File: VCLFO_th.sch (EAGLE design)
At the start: 38 parts, among them IC1 LM324N, IC3 LM358N

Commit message: Updated component values of LED2 and LDR1 (Vactrol/optocoupler).
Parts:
- LDR1: value PGM55xx 18-50k e-kit 40850005 -> Token PGM5539
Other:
- note added: "LED for LDR1 (DIY vactrol) Optosupply OSW50K57E1A White 5mm flat-front LED 2180-3000mcd"
- note removed: "LED for LDR1 (DIY vactrol)"
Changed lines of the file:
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@@
 <grid distance="0.1" unitdist="inch" unit="inch" style="lines" multiple="1" display="no" altdistance="0.01" altunitdist="inch" altunit="inch"/>
 <layers>
-<layer number="1" name="Top" color="4" fill="1" visible="yes" active="no"/>
-<layer number="16" name="Bottom" color="1" fill="1" visible="yes" active="no"/>
-<layer number="17" name="Pads" color="2" fill="1" visible="yes" active="no"/>
-<layer number="18" name="Vias" color="2" fill="1" visible="yes" active="no"/>
-<layer number="19" name="Unrouted" color="6" fill="1" visible="yes" active="no"/>
-<layer number="20" name="Dimension" color="15" fill="1" visible="yes" active="no"/>
-<layer number="21" name="tPlace" color="7" fill="1" visible="yes" active="no"/>
-<layer number="22" name="bPlace" color="7" fill="1" visible="yes" active="no"/>
-<layer number="23" name="tOrigins" color="15" fill="1" visible="yes" active="no"/>
-<layer number="24" name="bOrigins" color="15" fill="1" visible="yes" active="no"/>
-<layer number="25" name="tNames" color="7" fill="1" visible="yes" active="no"/>
-<layer number="26" name="bNames" color="7" fill="1" visible="yes" active="no"/>
-<layer number="27" name="tValues" color="7" fill="1" visible="yes" active="no"/>
-<layer number="28" name="bValues" color="7" fill="1" visible="yes" active="no"/>
+<layer number="1" name="Top" color="4" fill="1" visible="no" active="no"/>
+<layer number="16" name="Bottom" color="1" fill="1" visible="no" active="no"/>
+<layer number="17" name="Pads" color="2" fill="1" visible="no" active="no"/>
+<layer number="18" name="Vias" color="2" fill="1" visible="no" active="no"/>
+<layer number="19" name="Unrouted" color="6" fill="1" visible="no" active="no"/>
+<layer number="20" name="Dimension" color="15" fill="1" visible="no" active="no"/>
+<layer number="21" name="tPlace" color="7" fill="1" visible="no" active="no"/>
+<layer number="22" name="bPlace" color="7" fill="1" visible="no" active="no"/>
+<layer number="23" name="tOrigins" color="15" fill="1" visible="no" active="no"/>
+<layer number="24" name="bOrigins" color="15" fill="1" visible="no" active="no"/>
+<layer number="25" name="tNames" color="7" fill="1" visible="no" active="no"/>
+<layer number="26" name="bNames" color="7" fill="1" visible="no" active="no"/>
+<layer number="27" name="tValues" color="7" fill="1" visible="no" active="no"/>
+<layer number="28" name="bValues" color="7" fill="1" visible="no" active="no"/>
 <layer number="29" name="tStop" color="7" fill="3" visible="no" active="no"/>
 <layer number="30" name="bStop" color="7" fill="6" visible="no" active="no"/>
@@
 <layer number="35" name="tGlue" color="7" fill="4" visible="no" active="no"/>
 <layer number="36" name="bGlue" color="7" fill="5" visible="no" active="no"/>
-<layer number="37" name="tTest" color="7" fill="1" visible="yes" active="no"/>
-<layer number="38" name="bTest" color="7" fill="1" visible="yes" active="no"/>
+<layer number="37" name="tTest" color="7" fill="1" visible="no" active="no"/>
+<layer number="38" name="bTest" color="7" fill="1" visible="no" active="no"/>
 <layer number="39" name="tKeepout" color="4" fill="11" visible="no" active="no"/>
 <layer number="40" name="bKeepout" color="1" fill="11" visible="no" active="no"/>
@@
 <layer number="44" name="Drills" color="7" fill="1" visible="no" active="no"/>
 <layer number="45" name="Holes" color="7" fill="1" visible="no" active="no"/>
-<layer number="46" name="Milling" color="3" fill="1" visible="yes" active="no"/>
-<layer number="47" name="Measures" color="7" fill="1" visible="yes" active="no"/>
-<layer number="48" name="Document" color="7" fill="1" visible="yes" active="no"/>
-<layer number="49" name="Reference" color="7" fill="1" visible="yes" active="no"/>
-<layer number="50" name="dxf" color="7" fill="1" visible="yes" active="no"/>
-<layer number="51" name="tDocu" color="7" fill="1" visible="yes" active="no"/>
-<layer number="52" name="bDocu" color="7" fill="1" visible="yes" active="no"/>
-<layer number="53" name="tGND_GNDA" color="7" fill="1" visible="yes" active="no"/>
-<layer number="54" name="bGND_GNDA" color="7" fill="1" visible="yes" active="no"/>
-<layer number="56" name="wert" color="7" fill="1" visible="yes" active="no"/>
-<layer number="57" name="tCAD" color="7" fill="1" visible="yes" active="no"/>
+<layer number="46" name="Milling" color="3" fill="1" visible="no" active="no"/>
+<layer number="47" name="Measures" color="7" fill="1" visible="no" active="no"/>
+<layer number="48" name="Document" color="7" fill="1" visible="no" active="no"/>
+<layer number="49" name="Reference" color="7" fill="1" visible="no" active="no"/>
+<layer number="50" name="dxf" color="7" fill="1" visible="no" active="no"/>
+<layer number="51" name="tDocu" color="7" fill="1" visible="no" active="no"/>
+<layer number="52" name="bDocu" color="7" fill="1" visible="no" active="no"/>
+<layer number="53" name="tGND_GNDA" color="7" fill="1" visible="no" active="no"/>
+<layer number="54" name="bGND_GNDA" color="7" fill="1" visible="no" active="no"/>
+<layer number="56" name="wert" color="7" fill="1" visible="no" active="no"/>
+<layer number="57" name="tCAD" color="7" fill="1" visible="no" active="no"/>
 <layer number="90" name="Modules" color="5" fill="1" visible="yes" active="yes"/>
 <layer number="91" name="Nets" color="2" fill="1" visible="yes" active="yes"/>
@@
 <part name="D1" library="diode" deviceset="DIODE-" device="D-5" value="Diode 1A 50V"/>
 <part name="D2" library="diode" deviceset="DIODE-" device="D-5" value="Diode 1A 50V"/>
-<part name="LDR1" library="lb_devs" deviceset="LDR_TOKEN_PGM55XX" device="" value="PGM55xx 18-50k e-kit 40850005"/>
+<part name="LDR1" library="lb_devs" deviceset="LDR_TOKEN_PGM55XX" device="" value="Token PGM5539"/>
 <part name="TRI_LVL" library="pot-alps" deviceset="POT_US" device="VERTICAL" value="100k"/>
 <part name="SQR_LVL" library="pot-alps" deviceset="POT_US" device="VERTICAL" value="100k"/>
@@
 Mini toggle switch on-on
 Switch triangle to ramp wave</text>
-<text x="157.48" y="66.04" size="1.778" layer="91">LED for LDR1
-(DIY vactrol)</text>
+<text x="157.48" y="60.96" size="1.778" layer="91">LED for LDR1
+(DIY vactrol)
+Optosupply OSW50K57E1A
+White 5mm flat-front LED 2180-3000mcd</text>
 <text x="25.4" y="215.9" size="1.778" layer="91">S2 - Salecom sw SKS07SP
 Mini toggle switch on-off-on

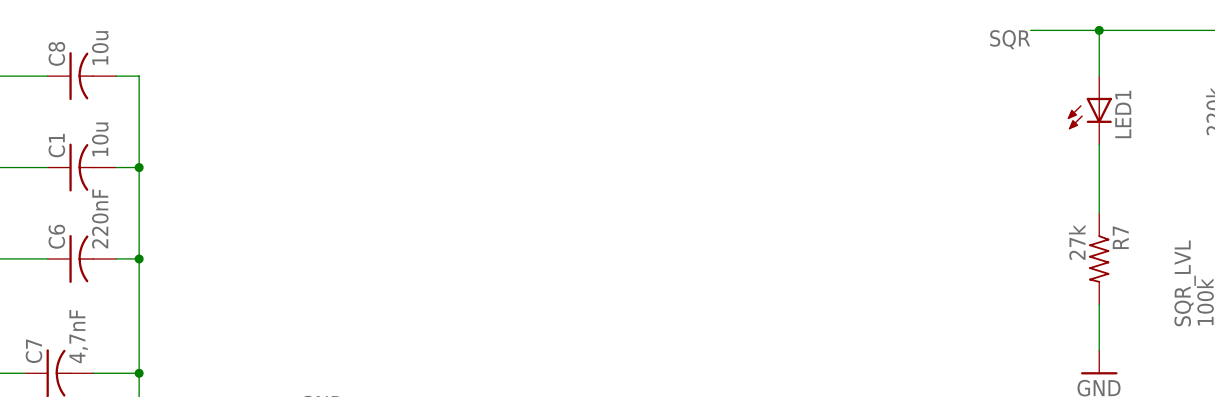
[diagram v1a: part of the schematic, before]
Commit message: Added comment about C1/C8.
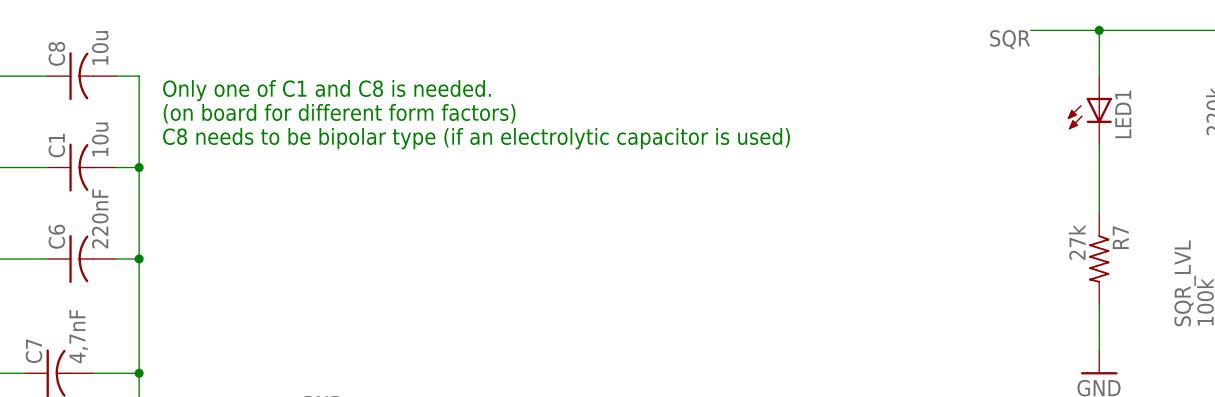
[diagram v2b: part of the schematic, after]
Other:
- note added: "Only one of C1 and C8 is needed. (on board for different form factors) C8 needs to be bipolar type (if an electrolytic capacitor is used)"
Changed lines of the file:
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@@
 Mini toggle switch on-off-on
 Oscillator rate range selector</text>
+<text x="86.36" y="218.44" size="1.778" layer="91">Only one of C1 and C8 is needed.
+(on board for different form factors)
+C8 needs to be bipolar type (if an electrolytic capacitor is used)</text>
 </plain>
 <instances>

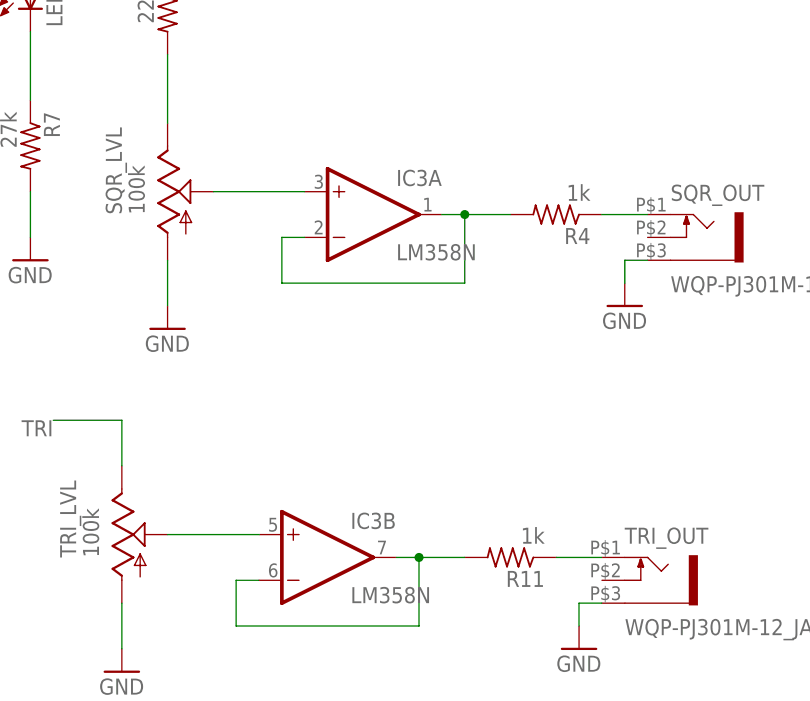
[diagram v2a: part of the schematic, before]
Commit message: Renamed IC3->IC2. Rate CV potentiometer was 1/40" off, corrected. Moved IC1 1/40" towards same pot, makes a bit more space for optical stuff. Moved R15 a bit, moved C6 and C7.
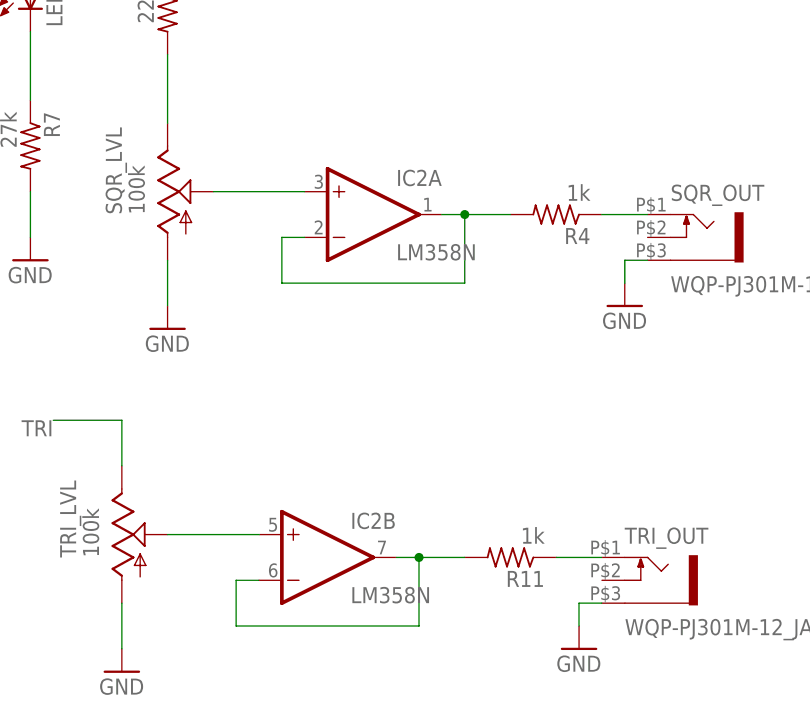
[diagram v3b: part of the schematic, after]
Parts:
- renumbered IC3 to IC2
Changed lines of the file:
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@@
 <part name="C5" library="rcl" deviceset="CPOL-US" device="E2.5-6" value="10u"/>
 <part name="C8" library="rcl" deviceset="C-US" device="025-050X050" value="10u"/>
-<part name="IC3" library="linear" deviceset="LM358" device="N"/>
+<part name="IC2" library="linear" deviceset="LM358" device="N"/>
 <part name="S3" library="switch" deviceset="TL36PO" device="" value="SKS04SP"/>
 </parts>
@@
 <instance part="C5" gate="G$1" x="276.86" y="68.58"/>
 <instance part="C8" gate="G$1" x="76.2" y="226.06" rot="R90"/>
-<instance part="IC3" gate="A" x="228.6" y="198.12"/>
-<instance part="IC3" gate="B" x="223.52" y="160.02"/>
-<instance part="IC3" gate="P" x="327.66" y="73.66"/>
+<instance part="IC2" gate="A" x="228.6" y="198.12"/>
+<instance part="IC2" gate="B" x="223.52" y="160.02"/>
+<instance part="IC2" gate="P" x="327.66" y="73.66"/>
 <instance part="S3" gate="BEF1" x="71.12" y="137.16" rot="R270"/>
 </instances>
@@
 <pinref part="D1" gate="G$1" pin="C"/>
 <pinref part="C4" gate="G$1" pin="+"/>
-<pinref part="IC3" gate="P" pin="V+"/>
+<pinref part="IC2" gate="P" pin="V+"/>
 </segment>
 <segment>
@@
 <pinref part="D2" gate="G$1" pin="A"/>
 <pinref part="C5" gate="G$1" pin="-"/>
-<pinref part="IC3" gate="P" pin="V-"/>
+<pinref part="IC2" gate="P" pin="V-"/>
 </segment>
 </net>
@@
 <wire x1="238.76" y1="160.02" x2="233.68" y2="160.02" width="0.1524" layer="91"/>
 <junction x="233.68" y="160.02"/>
-<pinref part="IC3" gate="B" pin="-IN"/>
-<pinref part="IC3" gate="B" pin="OUT"/>
+<pinref part="IC2" gate="B" pin="-IN"/>
+<pinref part="IC2" gate="B" pin="OUT"/>
 </segment>
 </net>
@@
 <wire x1="236.22" y1="198.12" x2="238.76" y2="198.12" width="0.1524" layer="91"/>
 <junction x="238.76" y="198.12"/>
-<pinref part="IC3" gate="A" pin="-IN"/>
-<pinref part="IC3" gate="A" pin="OUT"/>
+<pinref part="IC2" gate="A" pin="-IN"/>
+<pinref part="IC2" gate="A" pin="OUT"/>
 </segment>
 </net>
@@
 <pinref part="SQR_LVL" gate="G$1" pin="S"/>
 <wire x1="210.82" y1="200.66" x2="220.98" y2="200.66" width="0.1524" layer="91"/>
-<pinref part="IC3" gate="A" pin="+IN"/>
+<pinref part="IC2" gate="A" pin="+IN"/>
 </segment>
 </net>
@@
 <pinref part="TRI_LVL" gate="G$1" pin="S"/>
 <wire x1="215.9" y1="162.56" x2="205.74" y2="162.56" width="0.1524" layer="91"/>
-<pinref part="IC3" gate="B" pin="+IN"/>
-</segment>
-</net>
+<pinref part="IC2" gate="B" pin="+IN"/>
+</segment>
+</net>
